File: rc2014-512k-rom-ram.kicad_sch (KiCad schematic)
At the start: 14 parts, among them J1 RC2014_Bus, U1 SST39SF040, U2 AS6C4008-55PCN, U3 74LS139, U4 74LS74, U5 74LS670, U6 74LS670, U7 74LS138

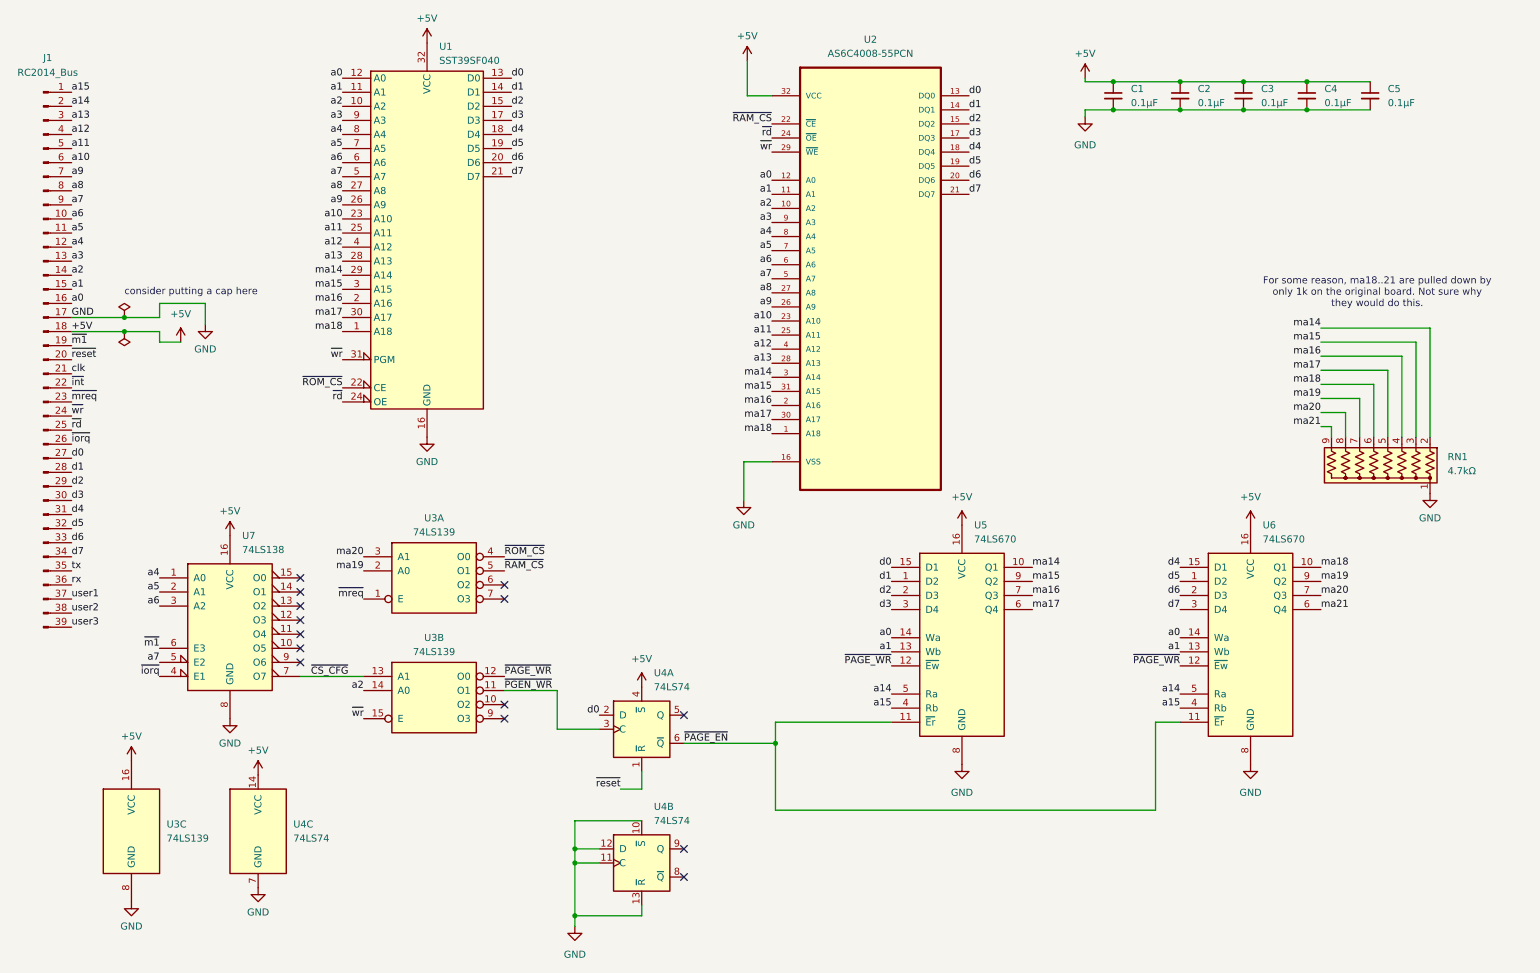
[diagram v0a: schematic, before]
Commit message: KiCad 9; fix designators
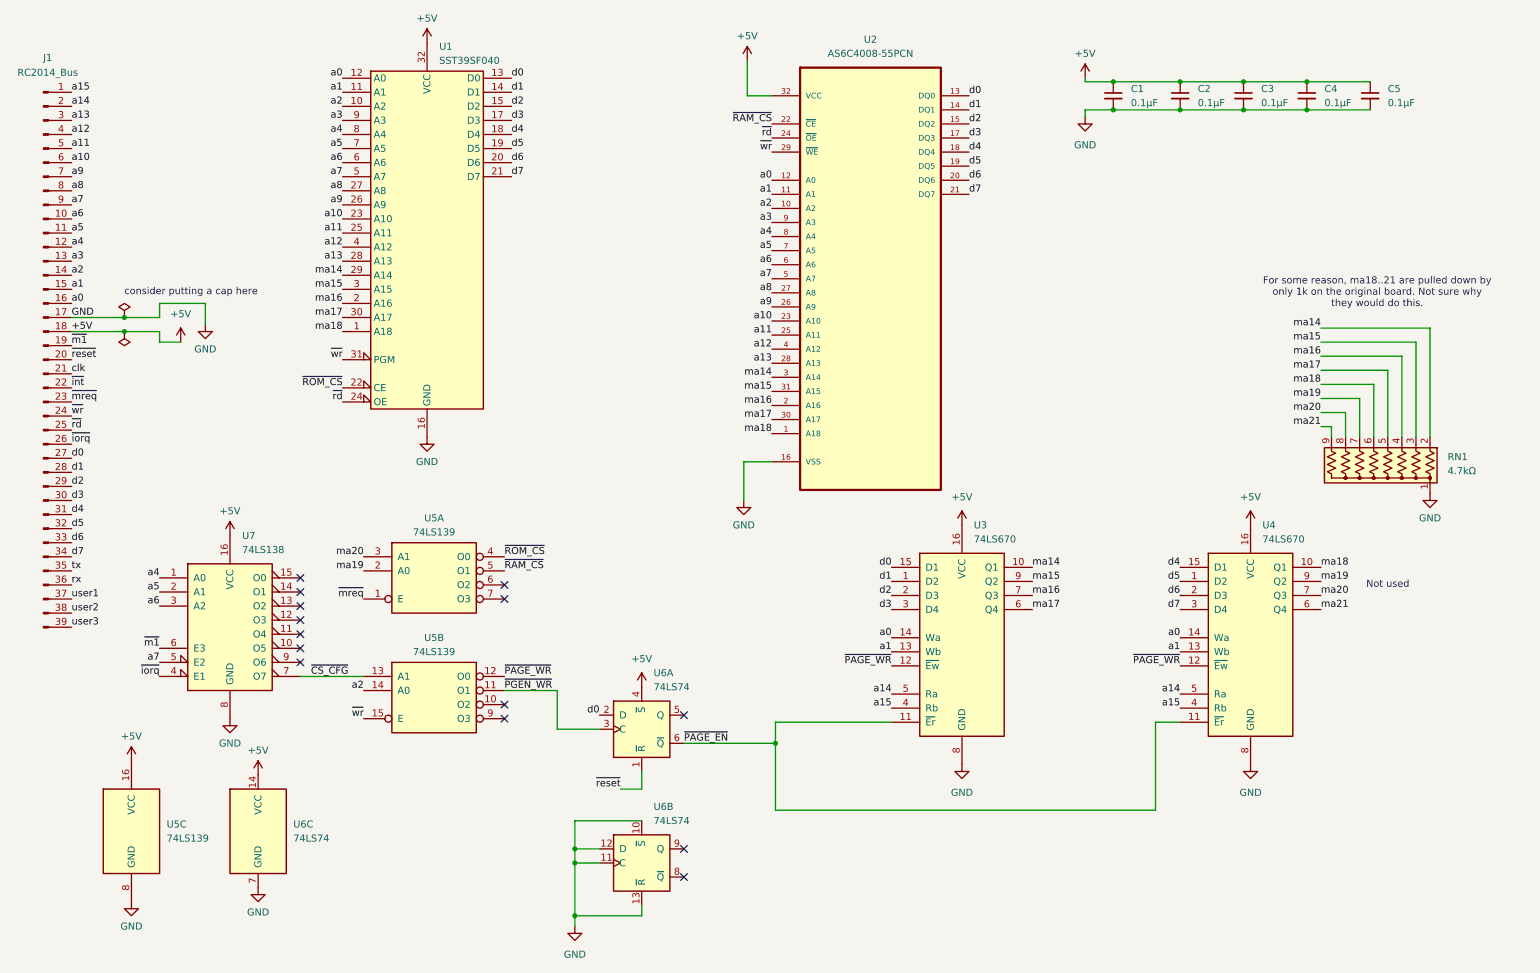
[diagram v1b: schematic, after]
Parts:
- renumbered U5 to U3, U6 to U4, U3 to U5, U4 to U6
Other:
- note added: "Not used"

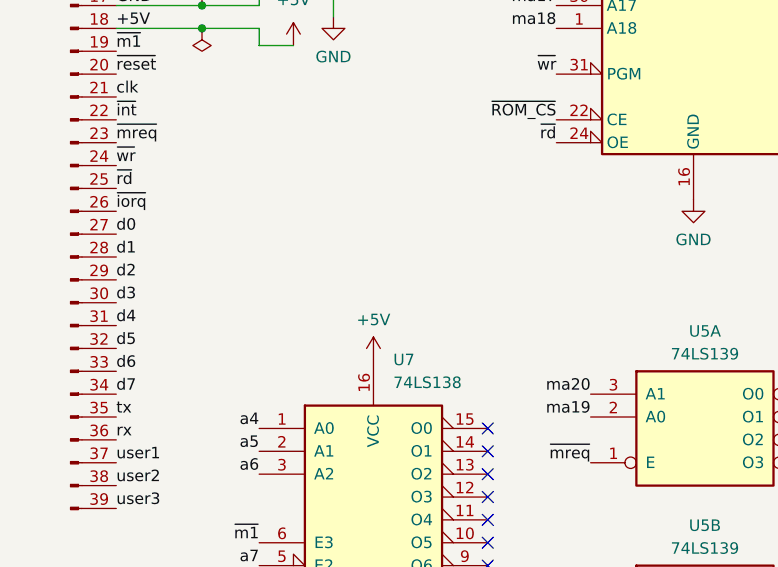
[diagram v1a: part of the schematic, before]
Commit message: Comments on memory map
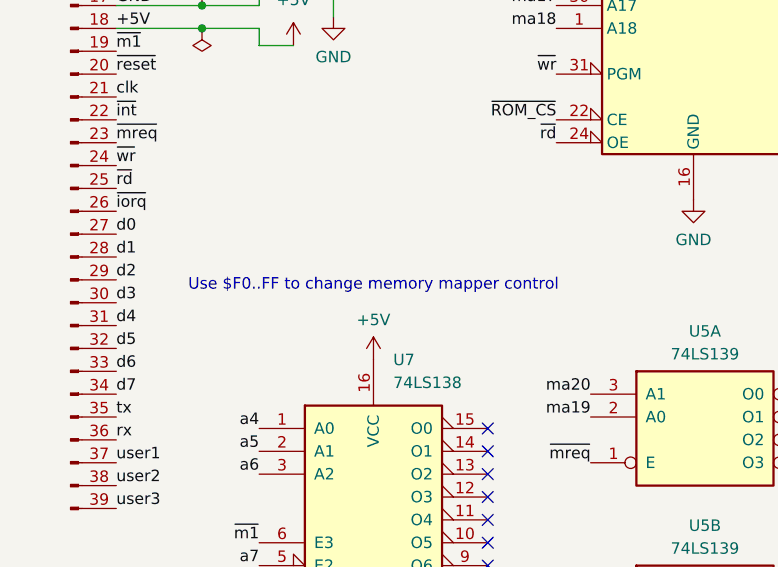
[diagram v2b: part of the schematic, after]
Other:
- note added: "Use $F0..FF to change memory mapper control"
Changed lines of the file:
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@@
+		)
+	)
+	(text "Use $F0..FF to change memory mapper control"
+		(exclude_from_sim no)
+		(at 52.07 99.06 0)
+		(effects
+			(font
+				(size 1.27 1.27)
+			)
 		)
 	)

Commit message: Big gate oops
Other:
- note added: "$78 and above for page config bits 1-5: page # (times two) bit 5: RAM, ~{ROM}"
- note added: "Use $70..7F to change memory mapper control"
- note removed: "Use $F0..FF to change memory mapper control"
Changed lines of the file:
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@@
 		)
 	)
-	(text "Use $F0..FF to change memory mapper control"
+	(text "Use $70..7F to change memory mapper control"
 		(exclude_from_sim no)
 		(at 52.07 99.06 0)
@@
 		)
 	)
+	(text "$78 and above for page config\nbits 1-5: page # (times two)\nbit 5: RAM, ~{ROM}"
+		(exclude_from_sim no)
+		(at 88.9 146.685 0)
+		(effects
+			(font
+				(size 1.27 1.27)
+			)
+		)
+	)
